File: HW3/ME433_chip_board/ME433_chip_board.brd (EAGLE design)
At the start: 25 parts

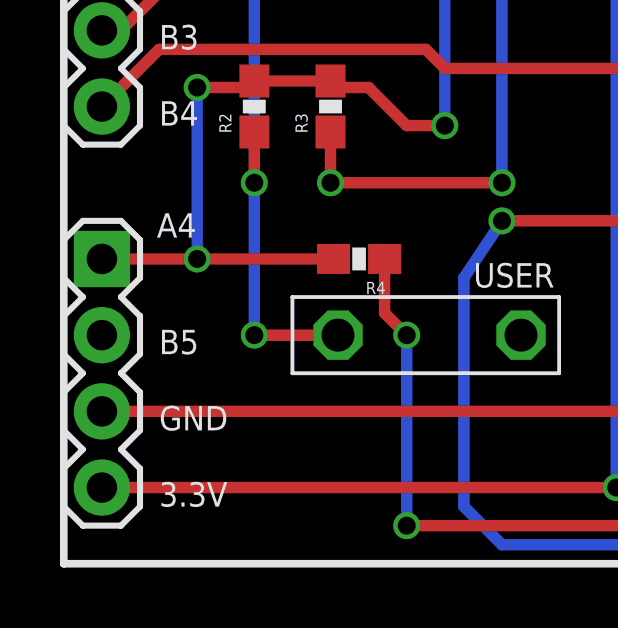
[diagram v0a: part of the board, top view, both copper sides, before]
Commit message: Fixed missing capacitor
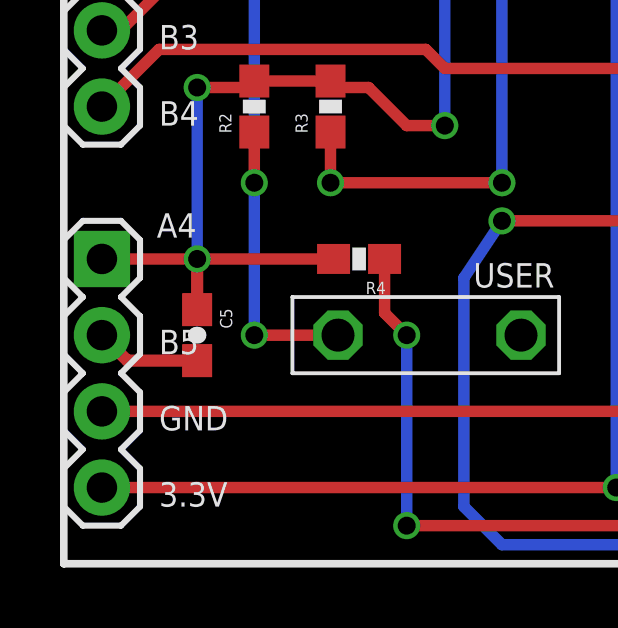
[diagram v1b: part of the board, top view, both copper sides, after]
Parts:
- added C5: (no value), ME433:0603-CAP
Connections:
- net 3.3V: now also C5.1
- net GND: now also C5.2
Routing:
- net GND: track 11.0 -> 14.6 mm
- net 3.3V: track 123.9 -> 125.6 mm
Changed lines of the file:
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@@
 <element name="U$3" library="ME433" package="2LEAD_PUSHBUTTON" value="2LEAD_PUSHBUTTON" x="21.59" y="2.2225"/>
 <element name="R4" library="SparkFun-Resistors" package="0603-RES" value="1k" x="9.8425" y="10.16" rot="R180"/>
+<element name="C5" library="ME433" package="0603-CAP" value="" x="4.445" y="7.62" rot="R270"/>
 </elements>
 <signals>
@@
 <wire x1="12.7" y1="27.94" x2="12.065" y2="28.575" width="0.381" layer="16"/>
 <contactref element="U$3" pad="A"/>
+<contactref element="C5" pad="2"/>
+<wire x1="4.445" y1="6.77" x2="2.12" y2="6.77" width="0.4064" layer="1"/>
+<wire x1="2.12" y1="6.77" x2="1.27" y2="7.62" width="0.4064" layer="1"/>
 </signal>
 <signal name="3.3V">
@@
 <contactref element="R4" pad="2"/>
 <wire x1="8.9925" y1="10.16" x2="4.445" y2="10.16" width="0.381" layer="1"/>
+<contactref element="C5" pad="1"/>
+<wire x1="4.445" y1="8.47" x2="4.445" y2="10.16" width="0.4064" layer="1"/>
 </signal>
 <signal name="B15">
